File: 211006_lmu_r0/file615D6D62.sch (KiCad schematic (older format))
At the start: 23 parts

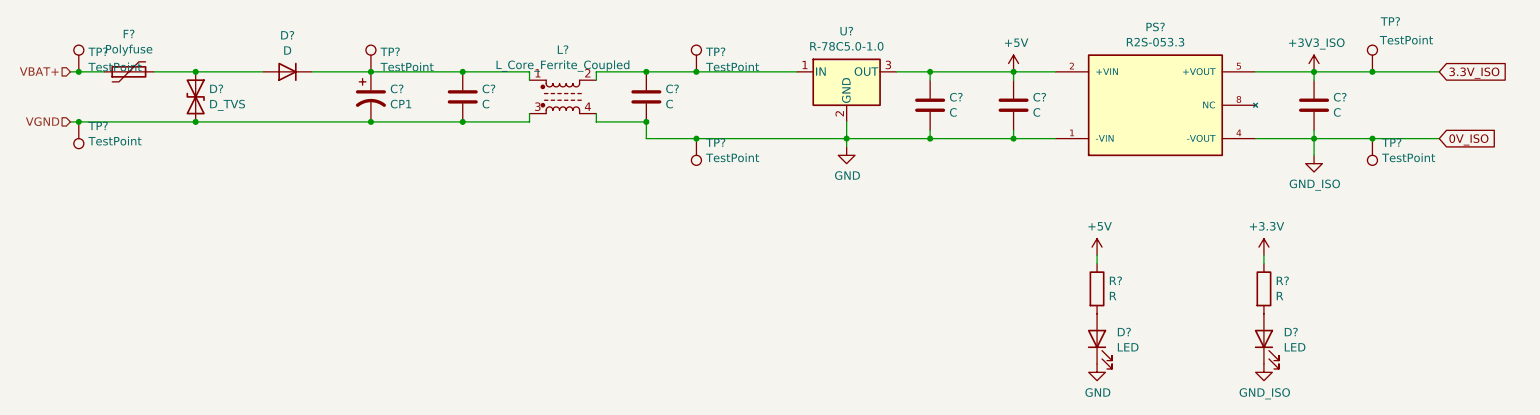
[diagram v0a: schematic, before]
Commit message: Updated BOM and footprints for non-hv components
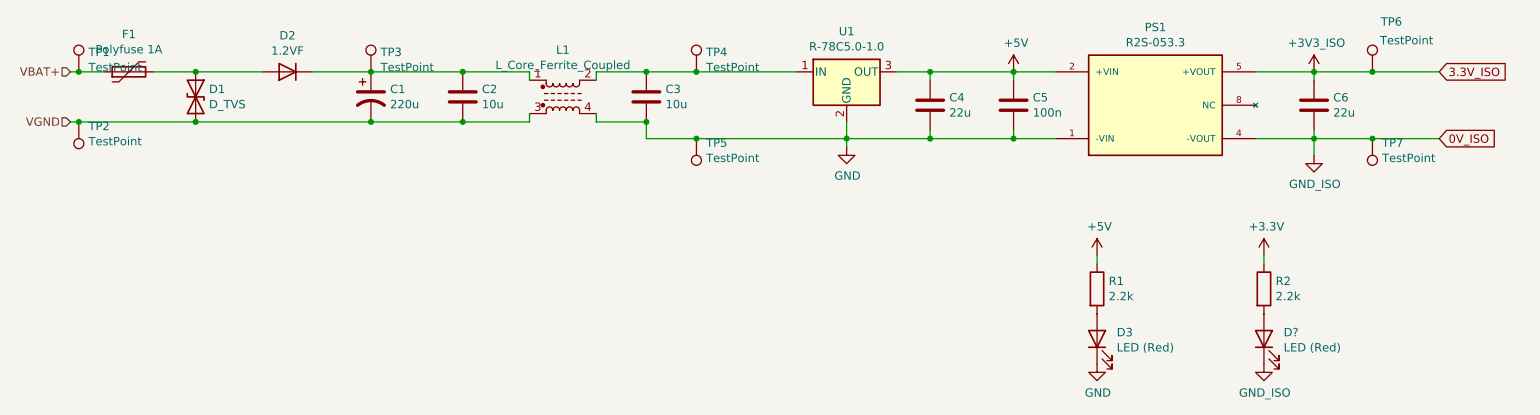
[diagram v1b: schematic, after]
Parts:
- removed D?: LED, symbol Device:LED
- added D?: LED (Red), LED_SMD:LED_0805_2012Metric_Pad1.15x1.40mm_HandSolder, symbol Device:LED
- C1: renamed from C?; value CP1 -> 220u; footprint (none) -> Capacitor_SMD:CP_Elec_10x12.5; Part Number (none) -> MAL214699106E3
- C2, C3: renamed from C?; value C -> 10u; footprint (none) -> Capacitor_SMD:C_0805_2012Metric_Pad1.18x1.45mm_HandSolder
- C4, C6: renamed from C?; value C -> 22u; footprint (none) -> Capacitor_SMD:C_0805_2012Metric_Pad1.18x1.45mm_HandSolder
- C5: renamed from C?; value C -> 100n; footprint (none) -> Capacitor_SMD:C_0603_1608Metric_Pad1.08x0.95mm_HandSolder
- D1: renamed from D?; footprint (none) -> Diode_SMD:D_SMB_Handsoldering; Manufacturer (none) -> Diodes Inc; Part Number (none) -> 1SMB5942B-13
- D2: renamed from D?; value D -> 1.2VF; footprint (none) -> Diode_SMD:D_SMB_Handsoldering; Manufacturer (none) -> SMC Diode Solutions; Part Number (none) -> SD560BTR
- D3: renamed from D?; value LED -> LED (Red); footprint (none) -> LED_SMD:LED_0805_2012Metric_Pad1.15x1.40mm_HandSolder
- F1: renamed from F?; value Polyfuse -> Polyfuse 1A; footprint (none) -> Fuse:Fuse_2920_7451Metric_Castellated; Manufacturer (none) -> Littelfuse; Part Number (none) -> 0ZCF0100AF2A
- L1: renamed from L?; footprint (none) -> Inductor_SMD:L_CommonModeChoke_Wuerth_WE-SL5; Part Number (none) -> 744272121
- R1, R2: renamed from R?; value R -> 2.2k; footprint (none) -> Resistor_SMD:R_0603_1608Metric_Pad0.98x0.95mm_HandSolder
- gave numbers to parts that had none: 9
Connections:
- net GND: now also D?.1 (K)
- net at R2.2: now also D?.2 (A)

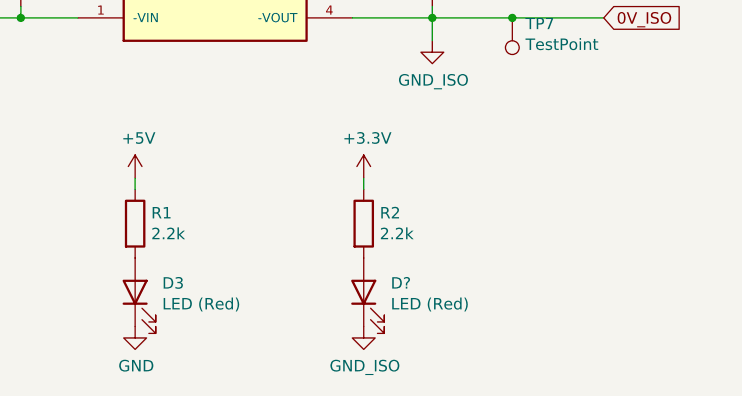
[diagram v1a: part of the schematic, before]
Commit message: Added most footprint requirements in HV
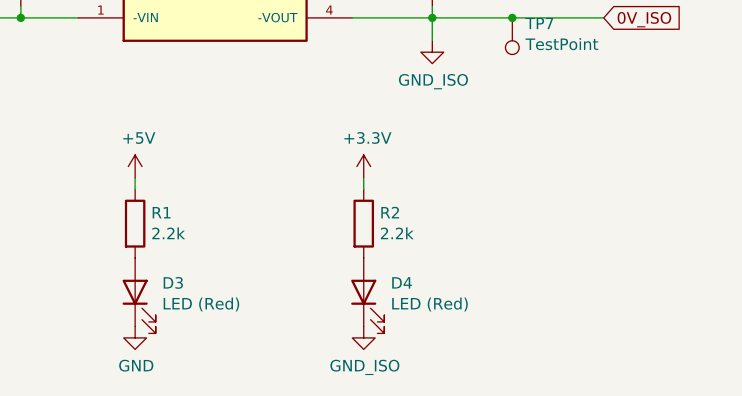
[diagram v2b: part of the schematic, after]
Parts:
- gave numbers to parts that had none: 1
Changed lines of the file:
@@
 Connection ~ 5350 2350
 $Comp
-L power:GND #PWR0102
+L power:GND #PWR02
 U 1 1 61665F18
 P 6550 2800
-F 0 "#PWR0102" H 6550 2550 50  0001 C CNN
+F 0 "#PWR02" H 6550 2550 50  0001 C CNN
 F 1 "GND" H 6555 2627 50  0000 C CNN
 F 2 "" H 6550 2800 50  0001 C CNN
@@
 $EndComp
 $Comp
-L power:+3.3V #PWR0103
+L power:+3.3V #PWR06
 U 1 1 6166EB6B
 P 9050 3450
-F 0 "#PWR0103" H 9050 3300 50  0001 C CNN
+F 0 "#PWR06" H 9050 3300 50  0001 C CNN
 F 1 "+3.3V" H 9065 3623 50  0000 C CNN
 F 2 "" H 9050 3450 50  0001 C CNN
@@
 $EndComp
 $Comp
-L power:GND #PWR0104
+L power:GND #PWR05
 U 1 1 616744B7
 P 8050 4100
-F 0 "#PWR0104" H 8050 3850 50  0001 C CNN
+F 0 "#PWR05" H 8050 3850 50  0001 C CNN
 F 1 "GND" H 8055 3927 50  0000 C CNN
 F 2 "" H 8050 4100 50  0001 C CNN
@@
 	9700 2750 9350 2750
 $Comp
-L power:+5V #PWR0105
+L power:+5V #PWR03
 U 1 1 6167A243
 P 7550 2350
-F 0 "#PWR0105" H 7550 2200 50  0001 C CNN
+F 0 "#PWR03" H 7550 2200 50  0001 C CNN
 F 1 "+5V" H 7565 2523 50  0000 C CNN
 F 2 "" H 7550 2350 50  0001 C CNN
@@
 $EndComp
 $Comp
-L power:+5V #PWR0106
+L power:+5V #PWR04
 U 1 1 6167A9D3
 P 8050 3450
-F 0 "#PWR0106" H 8050 3300 50  0001 C CNN
+F 0 "#PWR04" H 8050 3300 50  0001 C CNN
 F 1 "+5V" H 8065 3623 50  0000 C CNN
 F 2 "" H 8050 3450 50  0001 C CNN
@@
 Connection ~ 9700 2350
 $Comp
-L +3v3_iso:+3V3_ISO #PWR0107
+L +3v3_iso:+3V3_ISO #PWR08
 U 1 1 616407F5
 P 9350 2350
-F 0 "#PWR0107" H 9350 2200 50  0001 C CNN
+F 0 "#PWR08" H 9350 2200 50  0001 C CNN
 F 1 "+3V3_ISO" H 9365 2523 50  0000 C CNN
 F 2 "" H 9350 2350 50  0001 C CNN
@@
 	9350 2350 9700 2350
 $Comp
-L gnd_iso:GND_ISO #PWR0108
+L gnd_iso:GND_ISO #PWR09
 U 1 1 61642E17
 P 9350 2850
-F 0 "#PWR0108" H 9350 2600 50  0001 C CNN
+F 0 "#PWR09" H 9350 2600 50  0001 C CNN
 F 1 "GND_ISO" H 9355 2677 50  0000 C CNN
 F 2 "" H 9350 2850 50  0001 C CNN
@@
 $EndComp
 $Comp
-L gnd_iso:GND_ISO #PWR0109
+L gnd_iso:GND_ISO #PWR07
 U 1 1 616436D0
 P 9050 4100
-F 0 "#PWR0109" H 9050 3850 50  0001 C CNN
+F 0 "#PWR07" H 9050 3850 50  0001 C CNN
 F 1 "GND_ISO" H 9055 3927 50  0000 C CNN
 F 2 "" H 9050 4100 50  0001 C CNN
@@
 $EndComp
 $Comp
-L Device:LED D?
+L Device:LED D4
 U 1 1 61F45D3D
 P 9050 3950
-F 0 "D?" V 9089 3832 50  0000 R CNN
+F 0 "D4" V 9089 3832 50  0000 R CNN
 F 1 "LED (Red)" V 8998 3832 50  0000 R CNN
 F 2 "LED_SMD:LED_0805_2012Metric_Pad1.15x1.40mm_HandSolder" H 9050 3950 50  0001 C CNN

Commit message: Cleaned up last components missing footprint refs
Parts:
- TP1, TP2, TP3, TP4, TP5, TP6, TP7: footprint (none) -> TestPoint:TestPoint_Pad_D1.0mm
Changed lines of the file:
@@
 F 0 "TP4" H 5708 2468 50  0000 L CNN
 F 1 "TestPoint" H 5708 2377 50  0000 L CNN
-F 2 "" H 5850 2350 50  0001 C CNN
+F 2 "TestPoint:TestPoint_Pad_D1.0mm" H 5850 2350 50  0001 C CNN
 F 3 "~" H 5850 2350 50  0001 C CNN
 	1    5650 2350
@@
 F 0 "TP3" H 3758 2468 50  0000 L CNN
 F 1 "TestPoint" H 3758 2377 50  0000 L CNN
-F 2 "" H 3900 2350 50  0001 C CNN
+F 2 "TestPoint:TestPoint_Pad_D1.0mm" H 3900 2350 50  0001 C CNN
 F 3 "~" H 3900 2350 50  0001 C CNN
 	1    3700 2350
@@
 F 0 "TP1" H 2008 2468 50  0000 L CNN
 F 1 "TestPoint" H 2008 2377 50  0000 L CNN
-F 2 "" H 2150 2350 50  0001 C CNN
+F 2 "TestPoint:TestPoint_Pad_D1.0mm" H 2150 2350 50  0001 C CNN
 F 3 "~" H 2150 2350 50  0001 C CNN
 	1    1950 2350
@@
 F 0 "TP2" H 1892 2676 50  0000 R CNN
 F 1 "TestPoint" H 1892 2767 50  0000 R CNN
-F 2 "" H 2150 2650 50  0001 C CNN
+F 2 "TestPoint:TestPoint_Pad_D1.0mm" H 2150 2650 50  0001 C CNN
 F 3 "~" H 2150 2650 50  0001 C CNN
 	1    1950 2650
@@
 F 0 "TP5" H 5592 2776 50  0000 R CNN
 F 1 "TestPoint" H 5592 2867 50  0000 R CNN
-F 2 "" H 5850 2750 50  0001 C CNN
+F 2 "TestPoint:TestPoint_Pad_D1.0mm" H 5850 2750 50  0001 C CNN
 F 3 "~" H 5850 2750 50  0001 C CNN
 	1    5650 2750
@@
 F 0 "TP6" H 9750 2650 50  0000 L CNN
 F 1 "TestPoint" H 9745 2538 50  0000 L CNN
-F 2 "" H 9900 2350 50  0001 C CNN
+F 2 "TestPoint:TestPoint_Pad_D1.0mm" H 9900 2350 50  0001 C CNN
 F 3 "~" H 9900 2350 50  0001 C CNN
 	1    9700 2350
@@
 F 0 "TP7" H 9642 2776 50  0000 R CNN
 F 1 "TestPoint" H 9642 2867 50  0000 R CNN
-F 2 "" H 9900 2750 50  0001 C CNN
+F 2 "TestPoint:TestPoint_Pad_D1.0mm" H 9900 2750 50  0001 C CNN
 F 3 "~" H 9900 2750 50  0001 C CNN
 	1    9700 2750
